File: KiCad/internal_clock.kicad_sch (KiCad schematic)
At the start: 8 parts, among them U1 TL074

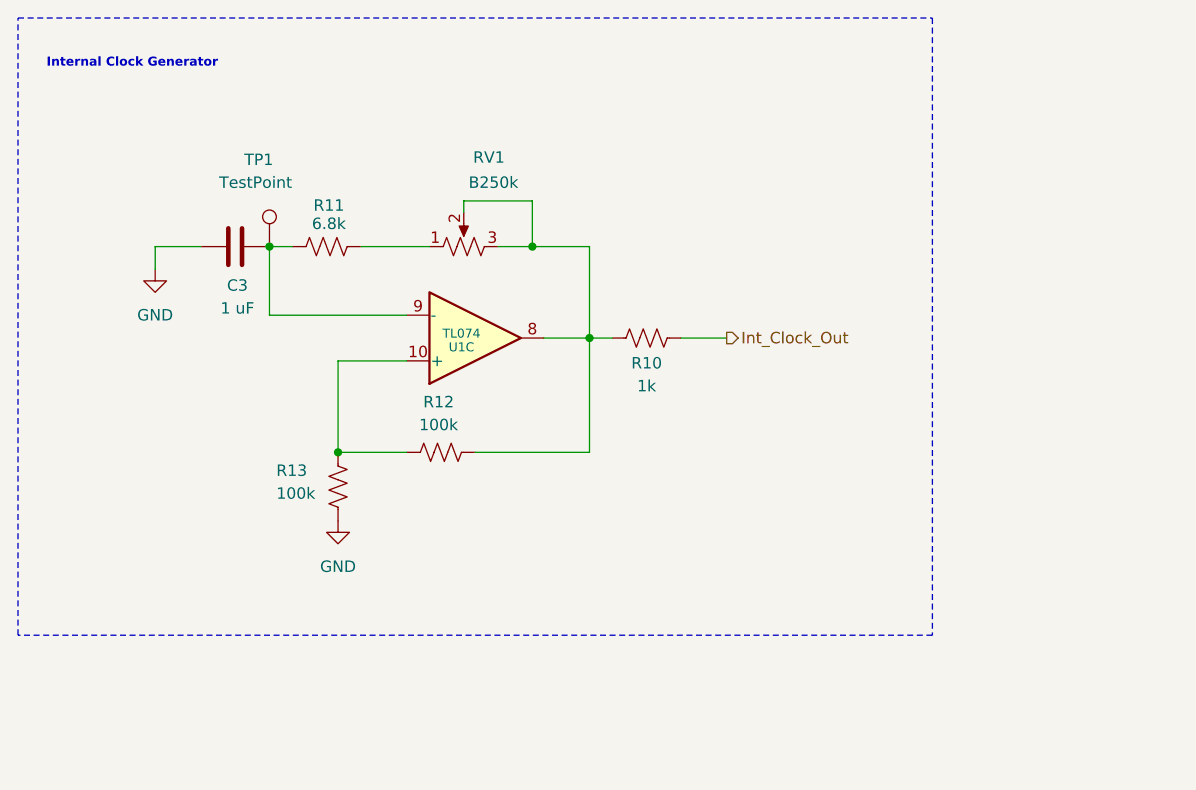
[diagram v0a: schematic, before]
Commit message: schematic: update cicada schematic
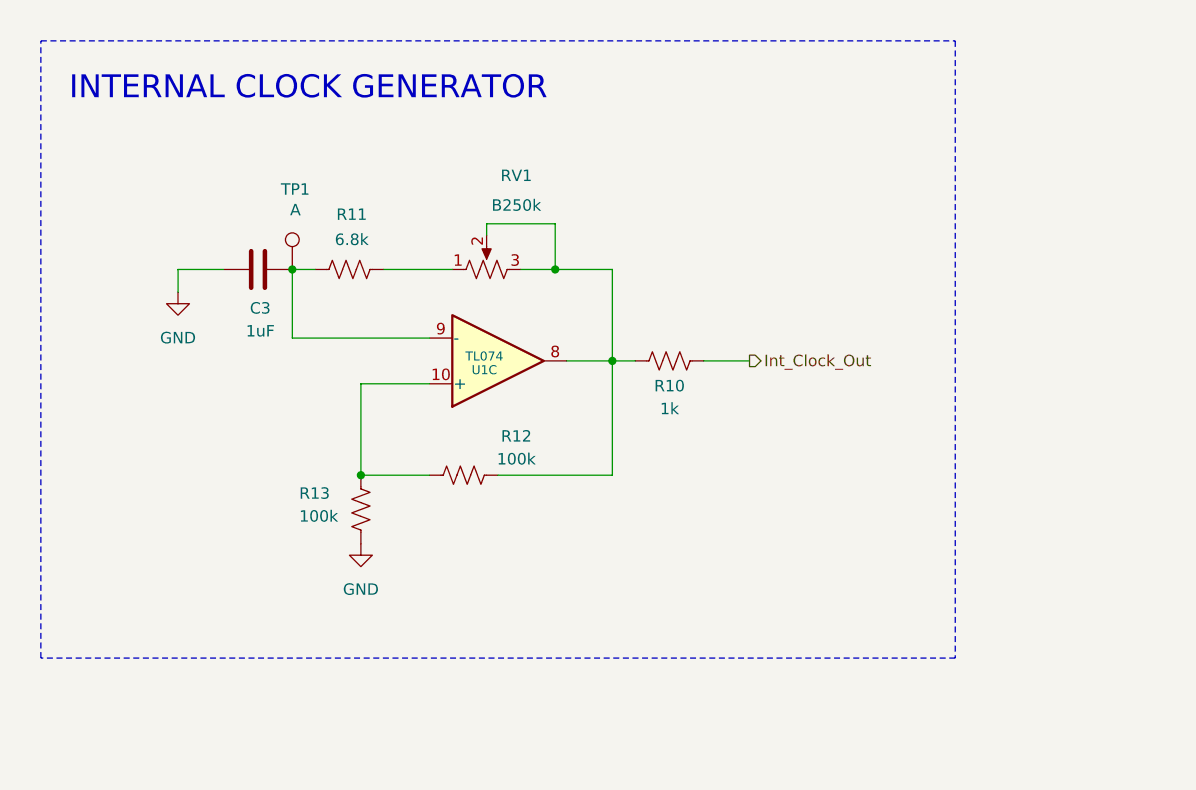
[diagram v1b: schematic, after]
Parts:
- C3: value 1 uF -> 1uF
- TP1: value TestPoint -> A
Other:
- note added: "INTERNAL CLOCK GENERATOR"
- note removed: "Internal Clock Generator"
- company: (none) -> Dirty Dream - Nathanael Noir
- title: (none) -> 8 Step Sequencer
- moved on the sheet: C3, R10, R11, R12, R13, RV1, TP1, U1C

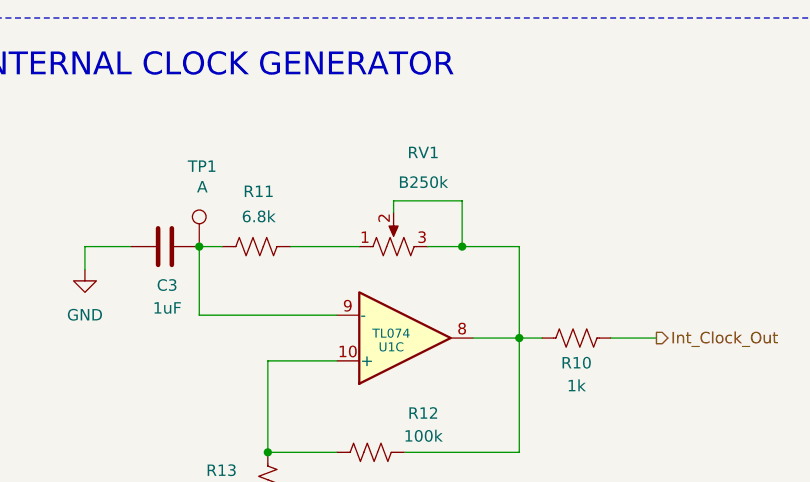
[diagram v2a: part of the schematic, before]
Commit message: adding missing SMD footprints
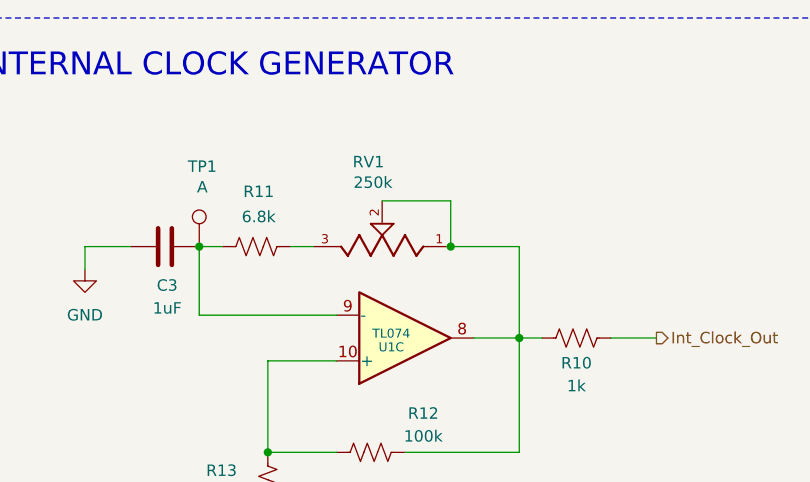
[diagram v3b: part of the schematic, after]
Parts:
- removed RV1: B250k, symbol Device:R_Potentiometer_US
- added RV1: 250k, Eurorack:RD901F, symbol Eurorack:RD901F
- C3: footprint (none) -> Capacitor_SMD:C_0805_2012Metric_Pad1.18x1.45mm_HandSolder
- R10, R11, R12, R13: footprint (none) -> Resistor_SMD:R_0805_2012Metric_Pad1.20x1.40mm_HandSolder
- TP1: footprint (none) -> TestPoint:TestPoint_Pad_D1.5mm
- U1: footprint (none) -> Package_SO:SOIC-14_3.9x8.7mm_P1.27mm
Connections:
- net at R10.2, R12.1, U1.8: now also RV1.1, RV1.2
- net at R11.1: now also RV1.3

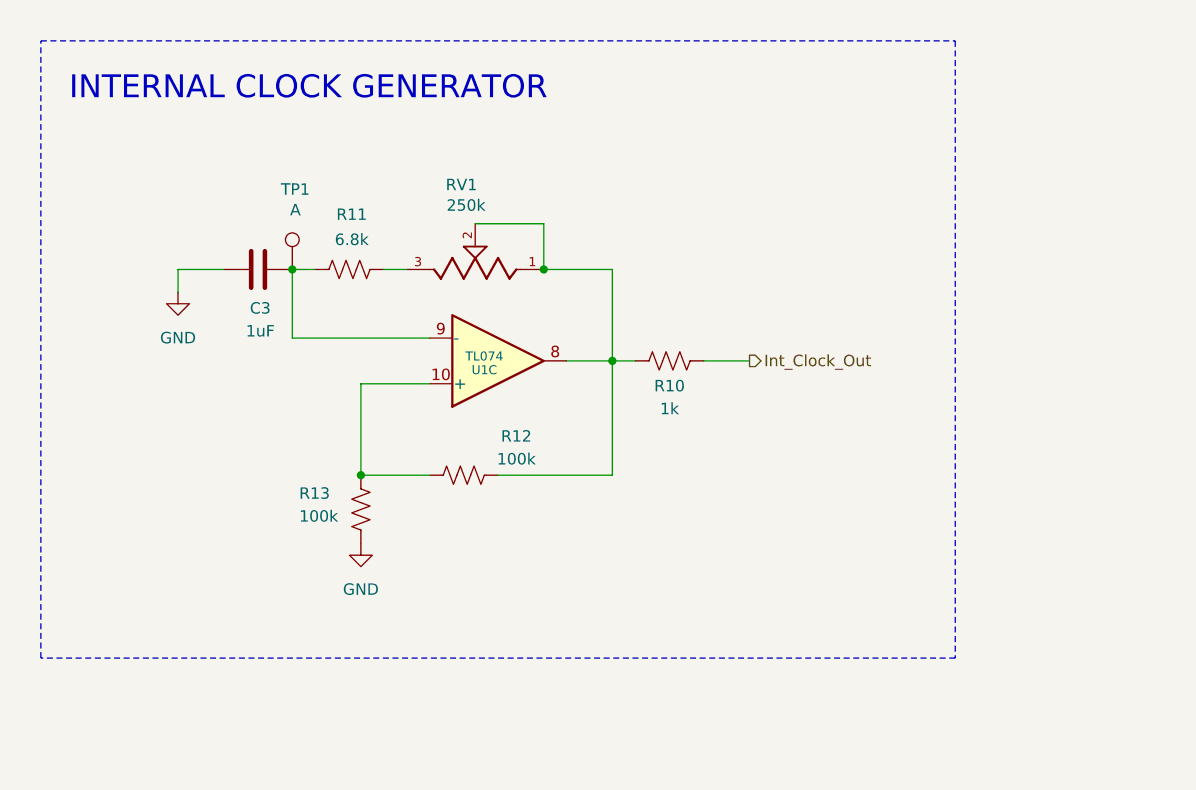
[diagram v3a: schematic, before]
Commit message: adding Test Point D
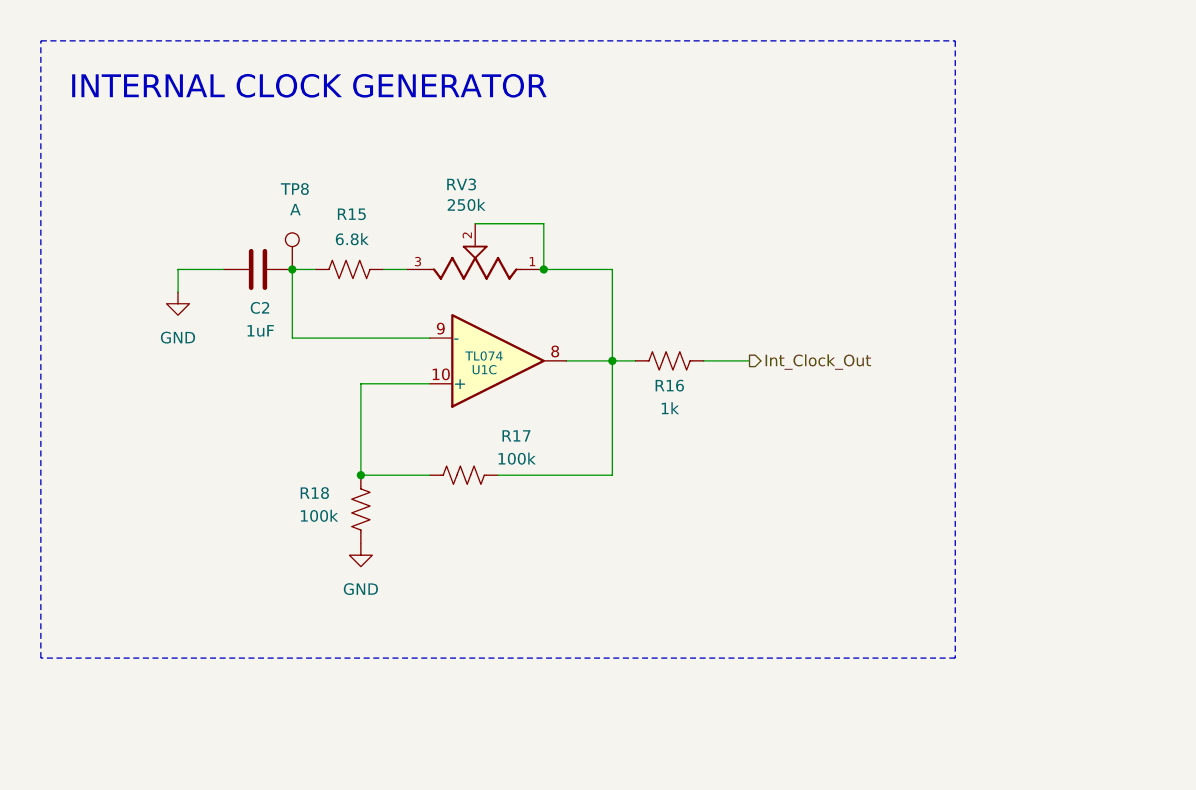
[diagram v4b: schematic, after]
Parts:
- renumbered C3 to C2, R11 to R15, R10 to R16, R12 to R17, R13 to R18, RV1 to RV3, TP1 to TP8
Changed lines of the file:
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@@
 		(dnp no)
 		(fields_autoplaced yes)
-		(property "Reference" "#PWR013"
+		(property "Reference" "#PWR018"
 			(at 55.88 82.55 0)
 			(effects
@@
 			(project "sequencer"
 				(path "/c997e785-a132-463f-bd08-a5a67a697207/b964167f-08d9-430a-9aa0-9a2613885304"
-					(reference "#PWR013")
+					(reference "#PWR018")
 					(unit 1)
 				)
@@
 		(on_board yes)
 		(dnp no)
-		(property "Reference" "R13"
+		(property "Reference" "R18"
 			(at 49.022 70.612 0)
 			(effects
@@
 			(project "sequencer"
 				(path "/c997e785-a132-463f-bd08-a5a67a697207/b964167f-08d9-430a-9aa0-9a2613885304"
-					(reference "R13")
+					(reference "R18")
 					(unit 1)
 				)
@@
 		(on_board yes)
 		(dnp no)
-		(property "Reference" "R10"
+		(property "Reference" "R16"
 			(at 90.17 58.674 90)
 			(effects
@@
 			(project "sequencer"
 				(path "/c997e785-a132-463f-bd08-a5a67a697207/b964167f-08d9-430a-9aa0-9a2613885304"
-					(reference "R10")
+					(reference "R16")
 					(unit 1)
 				)
@@
 		(dnp no)
 		(fields_autoplaced yes)
-		(property "Reference" "#PWR012"
+		(property "Reference" "#PWR017"
 			(at 35.56 54.61 0)
 			(effects
@@
 			(project "sequencer"
 				(path "/c997e785-a132-463f-bd08-a5a67a697207/b964167f-08d9-430a-9aa0-9a2613885304"
-					(reference "#PWR012")
+					(reference "#PWR017")
 					(unit 1)
 				)
@@
 		(on_board yes)
 		(dnp no)
-		(property "Reference" "R12"
+		(property "Reference" "R17"
 			(at 73.152 64.262 90)
 			(effects
@@
 			(project "sequencer"
 				(path "/c997e785-a132-463f-bd08-a5a67a697207/b964167f-08d9-430a-9aa0-9a2613885304"
-					(reference "R12")
+					(reference "R17")
 					(unit 1)
 				)
@@
 		(on_board yes)
 		(dnp no)
-		(property "Reference" "RV1"
+		(property "Reference" "RV3"
 			(at 67.056 36.322 0)
 			(effects
@@
 			(project ""
 				(path "/c997e785-a132-463f-bd08-a5a67a697207/b964167f-08d9-430a-9aa0-9a2613885304"
-					(reference "RV1")
+					(reference "RV3")
 					(unit 1)
 				)
@@
 		(on_board yes)
 		(dnp no)
-		(property "Reference" "TP1"
+		(property "Reference" "TP8"
 			(at 46.99 36.83 0)
 			(effects
@@
 			(project ""
 				(path "/c997e785-a132-463f-bd08-a5a67a697207/b964167f-08d9-430a-9aa0-9a2613885304"
-					(reference "TP1")
+					(reference "TP8")
 					(unit 1)
 				)
@@
 		(on_board yes)
 		(dnp no)
-		(property "Reference" "R11"
+		(property "Reference" "R15"
 			(at 54.864 39.624 90)
 			(effects
@@
 			(project "sequencer"
 				(path "/c997e785-a132-463f-bd08-a5a67a697207/b964167f-08d9-430a-9aa0-9a2613885304"
-					(reference "R11")
+					(reference "R15")
 					(unit 1)
 				)
@@
 		(on_board yes)
 		(dnp no)
-		(property "Reference" "C3"
+		(property "Reference" "C2"
 			(at 44.704 50.038 90)
 			(effects
@@
 			(project "sequencer"
 				(path "/c997e785-a132-463f-bd08-a5a67a697207/b964167f-08d9-430a-9aa0-9a2613885304"
-					(reference "C3")
+					(reference "C2")
 					(unit 1)
 				)

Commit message: initiating pcb layout
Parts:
- C2: footprint Capacitor_SMD:C_0805_2012Metric_Pad1.18x1.45mm_HandSolder -> Eurorack:Kemet Film Cap
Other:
- note added: "Use a 1 µF C0G/NP0 if available (rare/large); otherwise use a smaller C0G (100-470 nF) and scale the timing resistors accordingly."
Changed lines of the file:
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@@
 		(title "8 Step Sequencer")
 		(date "2026-03-13")
-		(rev "v0.0")
+		(rev "v1.0")
 		(company "Dirty Dream - Nathanael Noir")
 	)
 	(rectangle
 		(start 20.32 20.32)
-		(end 121.92 88.9)
+		(end 146.685 101.6)
 		(stroke
 			(width 0)
@@
 				(size 2.54 2.54)
 				(thickness 0.3175)
+			)
+		)
+	)
+	(text "Use a 1 µF C0G/NP0 if available (rare/large);\notherwise use a smaller C0G (100-470 nF) and scale the timing resistors accordingly.\n"
+		(exclude_from_sim no)
+		(at 81.026 92.71 0)
+		(effects
+			(font
+				(size 1.27 1.27)
 			)
 		)
@@
 			)
 		)
-		(property "Footprint" "Capacitor_SMD:C_0805_2012Metric_Pad1.18x1.45mm_HandSolder"
+		(property "Footprint" "Eurorack:Kemet Film Cap"
 			(at 48.26 44.7548 0)
 			(effects
@@
 			)
 		)
-		(property "Datasheet" "~"
+		(property "Datasheet" "https://www.mouser.it/ProductDetail/KEMET/R82DC4100AA60J?qs=Jv4FAWB%252B0HYVXjrTybqNAQ%3D%3D"
 			(at 44.45 45.72 0)
 			(effects

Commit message: placing layout frontview
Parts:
- RV3: footprint Eurorack:RD901F -> Eurorack:RD901F_1
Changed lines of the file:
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@@
 	(title_block
 		(title "8 Step Sequencer")
-		(date "2026-03-13")
+		(date "2026-03-21")
 		(rev "v1.0")
 		(company "Dirty Dream - Nathanael Noir")
@@
 			)
 		)
-		(property "Footprint" "Eurorack:RD901F"
+		(property "Footprint" "Eurorack:RD901F_1"
 			(at 68.58 45.72 0)
 			(effects
